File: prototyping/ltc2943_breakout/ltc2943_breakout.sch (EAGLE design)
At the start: 12 parts, among them U1 LTC2943

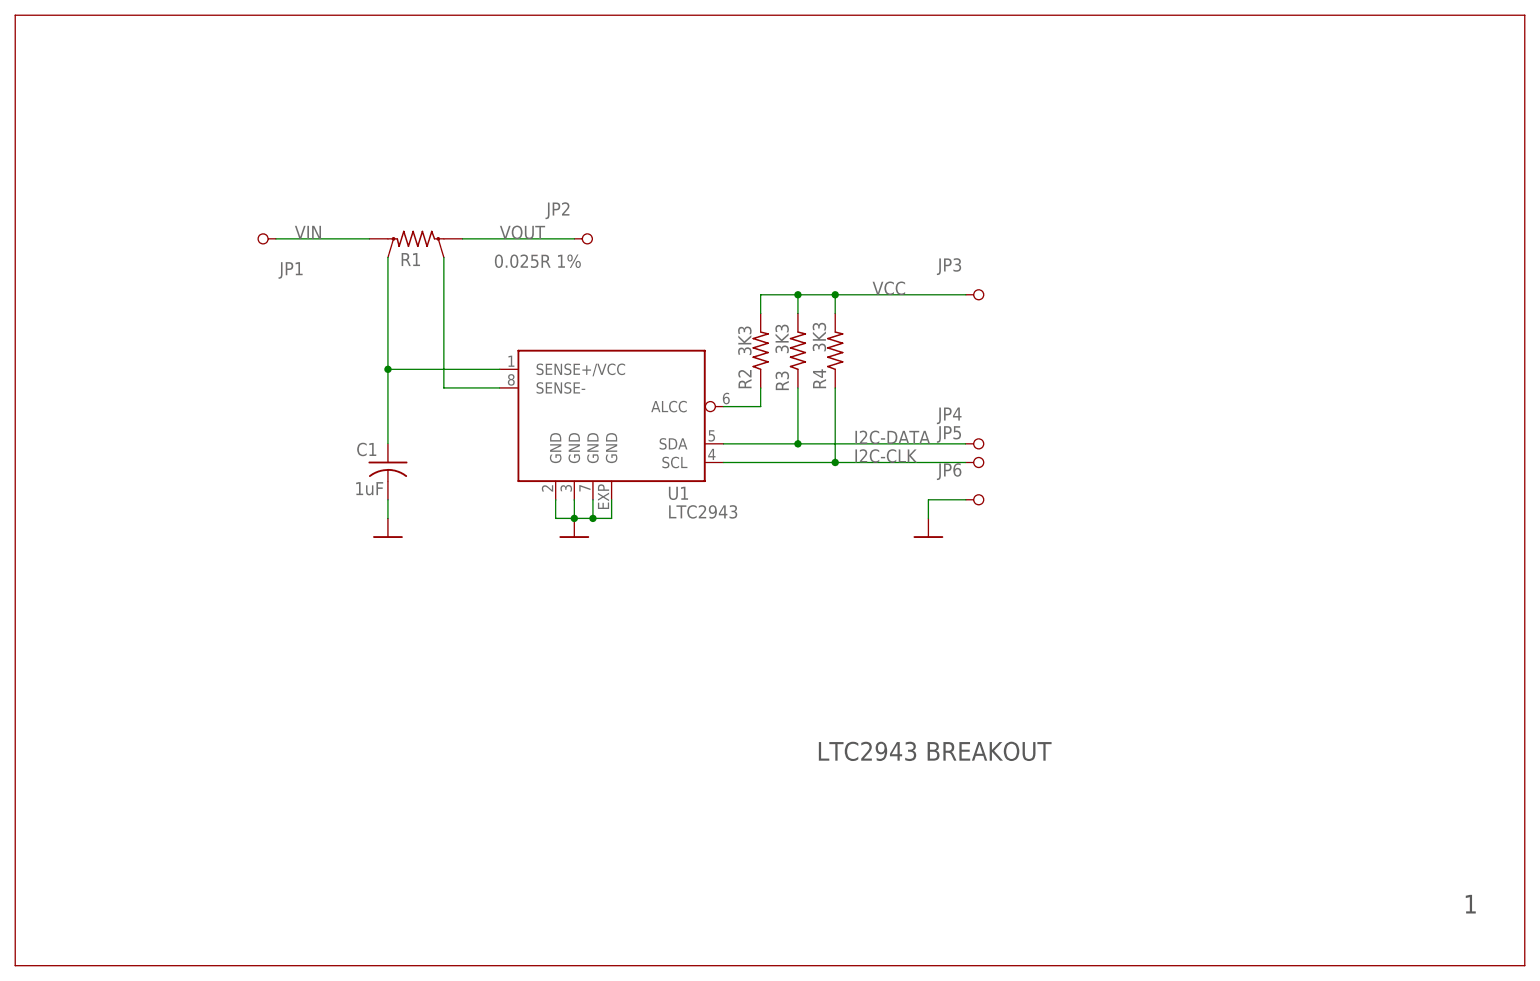
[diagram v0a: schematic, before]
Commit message: Updated ltc2943 breakout board.
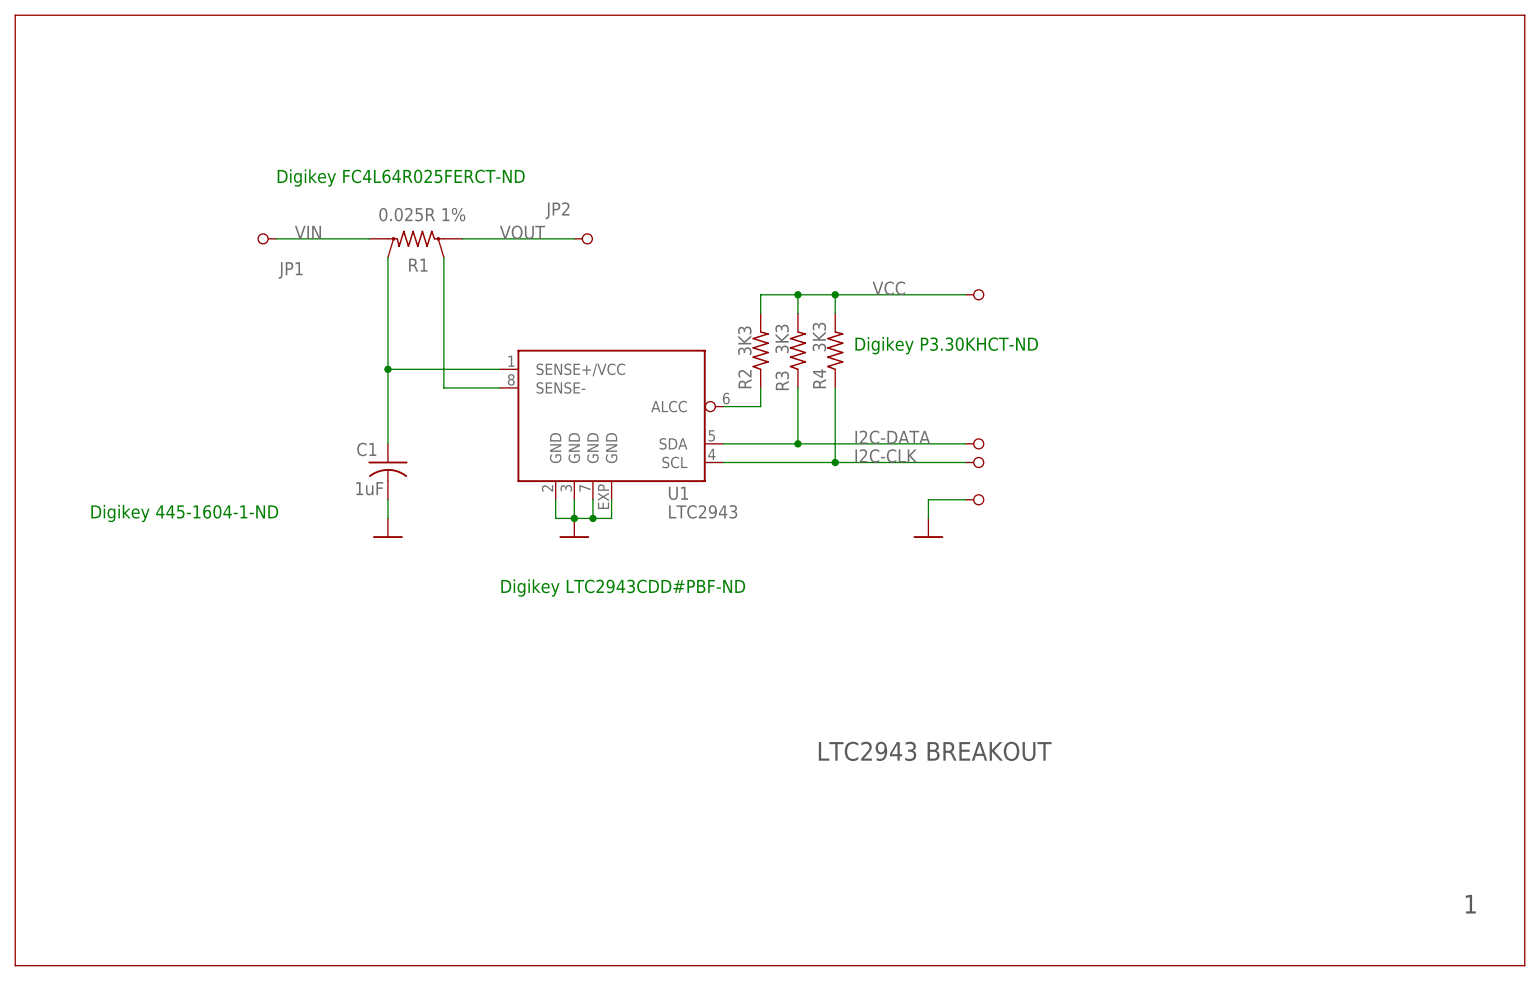
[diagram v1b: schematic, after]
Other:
- note added: "Digikey 445-1604-1-ND"
- note added: "Digikey FC4L64R025FERCT-ND"
- note added: "Digikey LTC2943CDD#PBF-ND"
- note added: "Digikey P3.30KHCT-ND"
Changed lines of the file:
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@@
 <wire x1="0" y1="0" x2="0" y2="129.54" width="0.1524" layer="94"/>
 <text x="197.358" y="7.112" size="2.54" layer="97">1</text>
+<text x="35.56" y="106.68" size="1.778" layer="91">Digikey FC4L64R025FERCT-ND </text>
+<text x="10.16" y="60.96" size="1.778" layer="91">Digikey 445-1604-1-ND </text>
+<text x="66.04" y="50.8" size="1.778" layer="91">Digikey LTC2943CDD#PBF-ND</text>
+<text x="114.3" y="83.82" size="1.778" layer="91">Digikey P3.30KHCT-ND </text>
 </plain>
 <instances>
@@
 </instance>
 <instance part="R1" gate="G$1" x="53.34" y="99.06" smashed="yes" rot="MR0">
-<attribute name="NAME" x="55.372" y="95.3516" size="1.778" layer="95" rot="MR0"/>
-<attribute name="VALUE" x="77.216" y="95.123" size="1.778" layer="96" rot="MR0"/>
+<attribute name="NAME" x="56.388" y="94.5896" size="1.778" layer="95" rot="MR0"/>
+<attribute name="VALUE" x="61.468" y="101.473" size="1.778" layer="96" rot="MR0"/>
 </instance>
 <instance part="R3" gate="G$1" x="106.68" y="83.82" smashed="yes" rot="R90">
@@
 <instance part="JP1" gate="G$1" x="33.02" y="99.06" rot="R180"/>
 <instance part="JP2" gate="G$1" x="78.74" y="99.06"/>
-<instance part="JP4" gate="G$1" x="132.08" y="71.12"/>
-<instance part="JP5" gate="G$1" x="132.08" y="68.58"/>
-<instance part="JP3" gate="G$1" x="132.08" y="91.44"/>
-<instance part="JP6" gate="G$1" x="132.08" y="63.5"/>
+<instance part="JP4" gate="G$1" x="132.08" y="71.12" smashed="yes"/>
+<instance part="JP5" gate="G$1" x="132.08" y="68.58" smashed="yes"/>
+<instance part="JP3" gate="G$1" x="132.08" y="91.44" smashed="yes"/>
+<instance part="JP6" gate="G$1" x="132.08" y="63.5" smashed="yes"/>
 <instance part="GND1" gate="1" x="124.46" y="58.42"/>
 </instances>
